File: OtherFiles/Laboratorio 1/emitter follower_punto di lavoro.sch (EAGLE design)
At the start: 3 parts

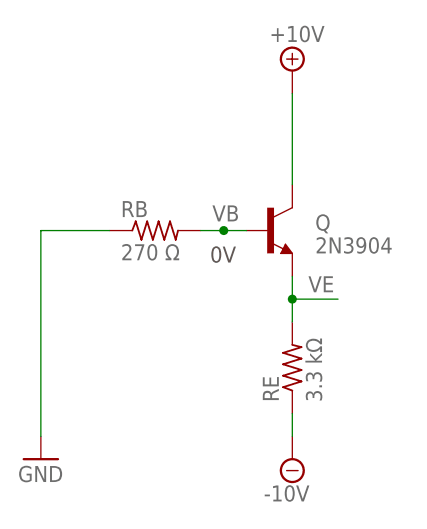
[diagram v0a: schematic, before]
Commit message: terminata analisi circuito laboratorio 1. da controllare dati e simboli
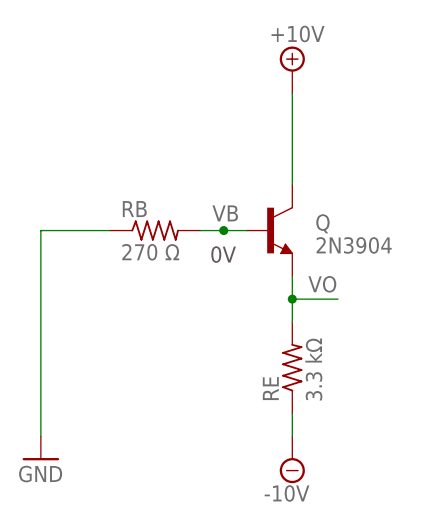
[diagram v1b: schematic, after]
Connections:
- net VE renamed VO
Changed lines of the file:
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@@
 </busses>
 <nets>
-<net name="VE" class="0">
+<net name="VO" class="0">
 <segment>
 <pinref part="RE" gate="G$1" pin="2"/>
